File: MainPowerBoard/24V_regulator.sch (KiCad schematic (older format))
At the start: 17 parts, among them U201 LMR16030S

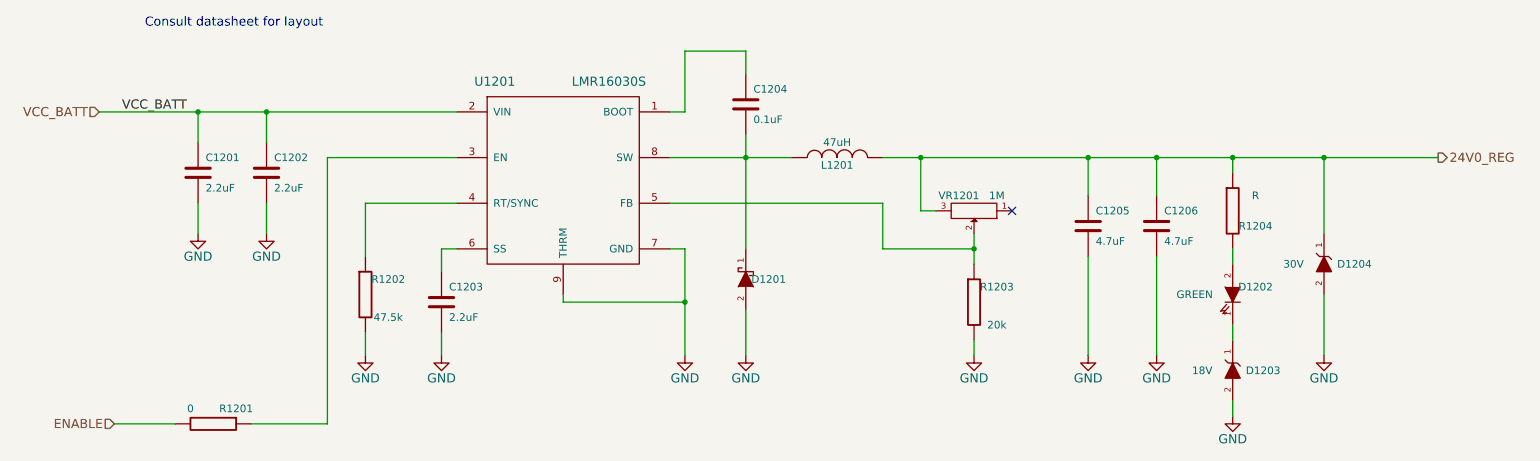
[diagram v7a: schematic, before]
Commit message: Placed all regulators on layout. Switched on-diode for SMT part.
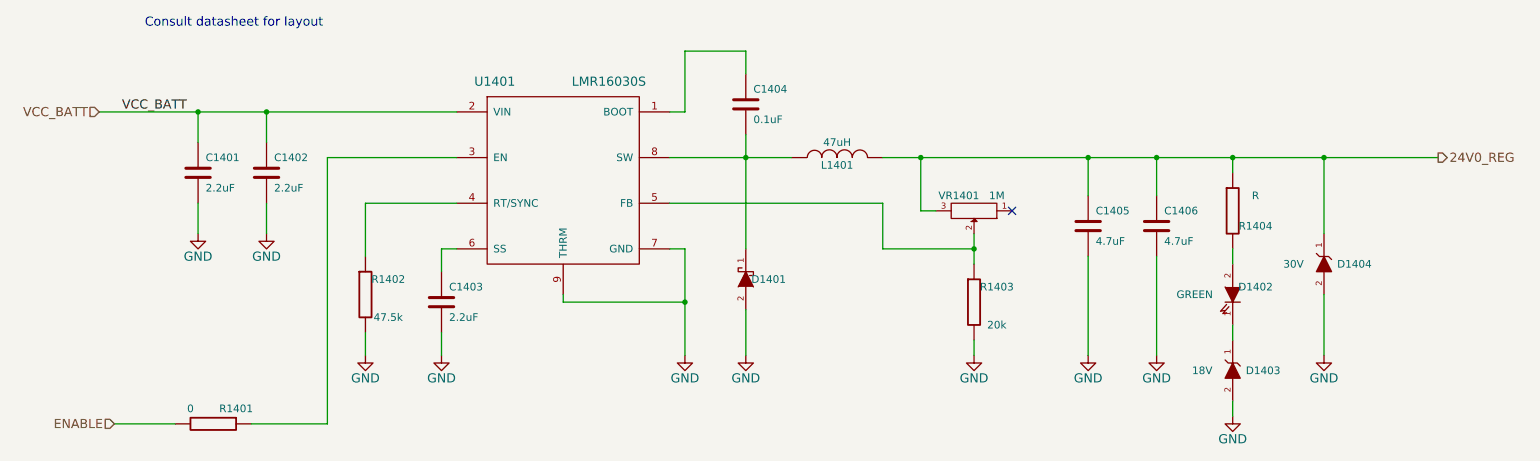
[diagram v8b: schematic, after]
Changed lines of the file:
@@
 LIBS:lmr16030s
 LIBS:tlc393
+LIBS:on-diode
 LIBS:MainPowerBoard-cache
 EELAYER 25 0
@@
 $Descr A 11000 8500
 encoding utf-8
-Sheet 2 14
+Sheet 14 14
 Title "Main Power Board"
 Date ""
@@
 AR Path="/583A9416/5833A728" Ref="R1304"  Part="1"
 AR Path="/583A941B/5833A728" Ref="R1404"  Part="1"
-F 0 "R1204" H 8750 3950 50  0000 C CNN
+F 0 "R1404" H 8750 3950 50  0000 C CNN
 F 1 "R" H 8750 4150 50  0000 C CNN
 F 2 "Resistors_SMD:R_1206_HandSoldering" V 8530 4050 30  0001 C CNN
@@
 AR Path="/583A9416/583A8678" Ref="U1301"  Part="1"
 AR Path="/583A941B/583A8678" Ref="U1401"  Part="1"
-F 0 "U1201" H 3750 4500 60  0000 C CNN
+F 0 "U1401" H 3750 4500 60  0000 C CNN
 F 1 "LMR16030S" H 4500 4500 60  0000 C CNN
 F 2 "hyperCustom:LMR16030S_8-PowerSOIC_TI" H 4150 3850 60  0001 C CNN
@@
 AR Path="/583A9416/583A8A9A" Ref="C1301"  Part="1"
 AR Path="/583A941B/583A8A9A" Ref="C1401"  Part="1"
-F 0 "C1201" H 1850 3900 50  0000 L CNN
+F 0 "C1401" H 1850 3900 50  0000 L CNN
 F 1 "2.2uF" H 1850 3700 50  0000 L CNN
 F 2 "Capacitors_SMD:C_1210_HandSoldering" H 1838 3650 30  0001 C CNN
@@
 AR Path="/583A9416/583A8B4B" Ref="C1302"  Part="1"
 AR Path="/583A941B/583A8B4B" Ref="C1402"  Part="1"
-F 0 "C1202" H 2300 3900 50  0000 L CNN
+F 0 "C1402" H 2300 3900 50  0000 L CNN
 F 1 "2.2uF" H 2300 3700 50  0000 L CNN
 F 2 "Capacitors_SMD:C_1210_HandSoldering" H 2288 3650 30  0001 C CNN
@@
 AR Path="/583A9416/583A8BF8" Ref="#PWR0101"  Part="1"
 AR Path="/583A941B/583A8BF8" Ref="#PWR0112"  Part="1"
-F 0 "#PWR090" H 1800 3950 60  0001 C CNN
+F 0 "#PWR0112" H 1800 3950 60  0001 C CNN
 F 1 "GND" H 1800 4050 60  0000 C CNN
 F 2 "" H 1800 4200 60  0000 C CNN
@@
 AR Path="/583A9416/583A8C28" Ref="#PWR0102"  Part="1"
 AR Path="/583A941B/583A8C28" Ref="#PWR0113"  Part="1"
-F 0 "#PWR091" H 2250 3950 60  0001 C CNN
+F 0 "#PWR0113" H 2250 3950 60  0001 C CNN
 F 1 "GND" H 2250 4050 60  0000 C CNN
 F 2 "" H 2250 4200 60  0000 C CNN
@@
 AR Path="/583A9416/583A8CF1" Ref="C1303"  Part="1"
 AR Path="/583A941B/583A8CF1" Ref="C1403"  Part="1"
-F 0 "C1203" H 3450 4750 50  0000 L CNN
+F 0 "C1403" H 3450 4750 50  0000 L CNN
 F 1 "2.2uF" H 3450 4550 50  0000 L CNN
 F 2 "Resistors_SMD:R_0805_HandSoldering" H 3438 4500 30  0001 C CNN
@@
 AR Path="/583A9416/583A8E72" Ref="#PWR0103"  Part="1"
 AR Path="/583A941B/583A8E72" Ref="#PWR0114"  Part="1"
-F 0 "#PWR092" H 2900 4750 60  0001 C CNN
+F 0 "#PWR0114" H 2900 4750 60  0001 C CNN
 F 1 "GND" H 2900 4850 60  0000 C CNN
 F 2 "" H 2900 5000 60  0000 C CNN
@@
 AR Path="/583A9416/583A8EBE" Ref="#PWR0104"  Part="1"
 AR Path="/583A941B/583A8EBE" Ref="#PWR0115"  Part="1"
-F 0 "#PWR093" H 3400 4750 60  0001 C CNN
+F 0 "#PWR0115" H 3400 4750 60  0001 C CNN
 F 1 "GND" H 3400 4850 60  0000 C CNN
 F 2 "" H 3400 5000 60  0000 C CNN
@@
 AR Path="/583A9416/583B27BB" Ref="#PWR0105"  Part="1"
 AR Path="/583A941B/583B27BB" Ref="#PWR0116"  Part="1"
-F 0 "#PWR094" H 5000 4750 60  0001 C CNN
+F 0 "#PWR0116" H 5000 4750 60  0001 C CNN
 F 1 "GND" H 5000 4850 60  0000 C CNN
 F 2 "" H 5000 5000 60  0000 C CNN
@@
 AR Path="/583A9416/583B2967" Ref="R1303"  Part="1"
 AR Path="/583A941B/583B2967" Ref="R1403"  Part="1"
-F 0 "R1203" H 7050 4750 50  0000 C CNN
+F 0 "R1403" H 7050 4750 50  0000 C CNN
 F 1 "20k" H 7050 4500 50  0000 C CNN
 F 2 "Resistors_SMD:R_1206_HandSoldering" V 6830 4650 30  0001 C CNN
@@
 AR Path="/583A9416/583B2A2E" Ref="VR1301"  Part="1"
 AR Path="/583A941B/583B2A2E" Ref="VR1401"  Part="1"
-F 0 "VR1201" H 7000 3950 50  0000 C CNN
+F 0 "VR1401" H 7000 3950 50  0000 C CNN
 F 1 "1M" H 6750 3950 50  0000 C CNN
 F 2 "hyperCustom:BOURNS_MULTITURNPOT_3299W" H 6900 4050 60  0001 C CNN
@@
 AR Path="/583A9416/583B2BCB" Ref="D1301"  Part="1"
 AR Path="/583A941B/583B2BCB" Ref="D1401"  Part="1"
-F 0 "D1201" V 5400 4350 50  0000 C CNN
+F 0 "D1401" V 5400 4350 50  0000 C CNN
 F 1 "DIODESCH" H 5400 4400 50  0001 C CNN
 F 2 "Diodes_SMD:SMA_Handsoldering" H 5400 4500 60  0001 C CNN
@@
 AR Path="/583A9416/583B2C66" Ref="#PWR0106"  Part="1"
 AR Path="/583A941B/583B2C66" Ref="#PWR0117"  Part="1"
-F 0 "#PWR095" H 5400 4750 60  0001 C CNN
+F 0 "#PWR0117" H 5400 4750 60  0001 C CNN
 F 1 "GND" H 5400 4850 60  0000 C CNN
 F 2 "" H 5400 5000 60  0000 C CNN
@@
 AR Path="/583A9416/583B2D59" Ref="L1301"  Part="1"
 AR Path="/583A941B/583B2D59" Ref="L1401"  Part="1"
-F 0 "L1201" V 5950 3700 50  0000 C CNN
+F 0 "L1401" V 5950 3700 50  0000 C CNN
 F 1 "47uH" V 6100 3700 50  0000 C CNN
 F 2 "hyperCustom:47uIND_CDRH127_LDNP-470MC_SUMIDA" H 6000 3700 60  0001 C CNN
@@
 AR Path="/583A9416/583B307C" Ref="#PWR0107"  Part="1"
 AR Path="/583A941B/583B307C" Ref="#PWR0118"  Part="1"
-F 0 "#PWR096" H 6900 4750 60  0001 C CNN
+F 0 "#PWR0118" H 6900 4750 60  0001 C CNN
 F 1 "GND" H 6900 4850 60  0000 C CNN
 F 2 "" H 6900 5000 60  0000 C CNN
@@
 AR Path="/583A9416/583B399E" Ref="C1304"  Part="1"
 AR Path="/583A941B/583B399E" Ref="C1404"  Part="1"
-F 0 "C1204" H 5450 3450 50  0000 L CNN
+F 0 "C1404" H 5450 3450 50  0000 L CNN
 F 1 "0.1uF" H 5450 3250 50  0000 L CNN
 F 2 "Resistors_SMD:R_1206_HandSoldering" H 5438 3200 30  0001 C CNN
@@
 AR Path="/583A9416/583B4188" Ref="C1305"  Part="1"
 AR Path="/583A941B/583B4188" Ref="C1405"  Part="1"
-F 0 "C1205" H 7700 4250 50  0000 L CNN
+F 0 "C1405" H 7700 4250 50  0000 L CNN
 F 1 "4.7uF" H 7700 4050 50  0000 L CNN
 F 2 "Capacitors_SMD:C_1206_HandSoldering" H 7688 4000 30  0001 C CNN
@@
 AR Path="/583A9416/583B42A9" Ref="#PWR0108"  Part="1"
 AR Path="/583A941B/583B42A9" Ref="#PWR0119"  Part="1"
-F 0 "#PWR097" H 7650 4750 60  0001 C CNN
+F 0 "#PWR0119" H 7650 4750 60  0001 C CNN
 F 1 "GND" H 7650 4850 60  0000 C CNN
 F 2 "" H 7650 5000 60  0000 C CNN
@@
 AR Path="/583A9416/583B43AD" Ref="C1306"  Part="1"
 AR Path="/583A941B/583B43AD" Ref="C1406"  Part="1"
-F 0 "C1206" H 8150 4250 50  0000 L CNN
+F 0 "C1406" H 8150 4250 50  0000 L CNN
 F 1 "4.7uF" H 8150 4050 50  0000 L CNN
 F 2 "Capacitors_SMD:C_1206_HandSoldering" H 8138 4000 30  0001 C CNN
@@
 AR Path="/583A9416/583B449E" Ref="#PWR0109"  Part="1"
 AR Path="/583A941B/583B449E" Ref="#PWR0120"  Part="1"
-F 0 "#PWR098" H 8100 4750 60  0001 C CNN
+F 0 "#PWR0120" H 8100 4750 60  0001 C CNN
 F 1 "GND" H 8100 4850 60  0000 C CNN
 F 2 "" H 8100 5000 60  0000 C CNN
@@
 AR Path="/583A9416/583D36BC" Ref="R1301"  Part="1"
 AR Path="/583A941B/583D36BC" Ref="R1401"  Part="1"
-F 0 "R1201" V 1800 5600 50  0000 C CNN
+F 0 "R1401" V 1800 5600 50  0000 C CNN
 F 1 "0" V 1800 5300 50  0000 C CNN
 F 2 "Resistors_SMD:R_1206_HandSoldering" V 1830 5450 30  0001 C CNN
@@
 AR Path="/583A9416/583D8D48" Ref="D1303"  Part="1"
 AR Path="/583A941B/583D8D48" Ref="D1403"  Part="1"
-F 0 "D1203" V 8600 4900 50  0000 C CNN
+F 0 "D1403" V 8600 4900 50  0000 C CNN
 F 1 "18V" V 8600 5300 50  0000 C CNN
 F 2 "Diodes_SMD:SMA_Handsoldering" H 8600 5100 60  0001 C CNN
@@
 AR Path="/583A9416/583D8F40" Ref="#PWR0110"  Part="1"
 AR Path="/583A941B/583D8F40" Ref="#PWR0121"  Part="1"
-F 0 "#PWR099" H 8600 5150 60  0001 C CNN
+F 0 "#PWR0121" H 8600 5150 60  0001 C CNN
 F 1 "GND" H 8600 5250 60  0000 C CNN
 F 2 "" H 8600 5400 60  0000 C CNN
@@
 AR Path="/583A9416/583D986C" Ref="D1304"  Part="1"
 AR Path="/583A941B/583D986C" Ref="D1404"  Part="1"
-F 0 "D1204" V 9200 4200 50  0000 C CNN
+F 0 "D1404" V 9200 4200 50  0000 C CNN
 F 1 "30V" V 9200 4600 50  0000 C CNN
 F 2 "Diodes_SMD:SMB_Handsoldering" H 9200 4400 60  0001 C CNN
@@
 AR Path="/583A9416/583D98F6" Ref="#PWR0111"  Part="1"
 AR Path="/583A941B/583D98F6" Ref="#PWR0122"  Part="1"
-F 0 "#PWR0100" H 9200 4750 60  0001 C CNN
+F 0 "#PWR0122" H 9200 4750 60  0001 C CNN
 F 1 "GND" H 9200 4850 60  0000 C CNN
 F 2 "" H 9200 5000 60  0000 C CNN
@@
 AR Path="/583A9416/583E258D" Ref="R1302"  Part="1"
 AR Path="/583A941B/583E258D" Ref="R1402"  Part="1"
-F 0 "R1202" H 3050 4700 50  0000 C CNN
+F 0 "R1402" H 3050 4700 50  0000 C CNN
 F 1 "47.5k" H 3050 4450 50  0000 C CNN
 F 2 "Resistors_SMD:R_1206_HandSoldering" V 2830 4600 30  0001 C CNN
@@
 AR Path="/583A9416/583D0112" Ref="D1302"  Part="1"
 AR Path="/583A941B/583D0112" Ref="D1402"  Part="1"
-F 0 "D1202" V 8550 4750 50  0000 C CNN
+F 0 "D1402" V 8550 4750 50  0000 C CNN
 F 1 "GREEN" V 8600 4350 50  0000 C CNN
 F 2 "LEDs:LED_1206" H 8600 4600 60  0001 C CNN
